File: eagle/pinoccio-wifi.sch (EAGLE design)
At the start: 23 parts, among them J1 AVR_SPI_PRG_6, J2 AVR_SPI_PRG_6, U1 GS1011MIPS, U2 M25PX16, U3 M25PX16, U4 TPS73533, U5 ATTINY13A

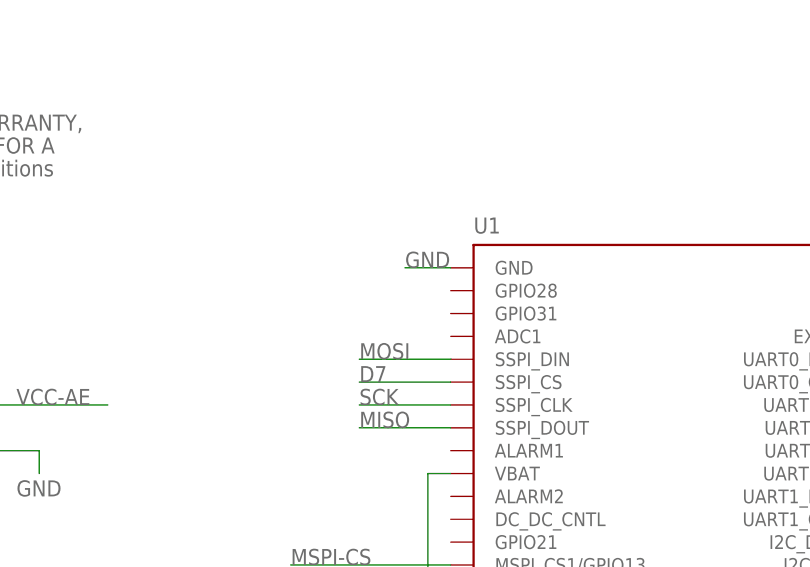
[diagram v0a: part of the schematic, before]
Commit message: Add data-ready trace to D5
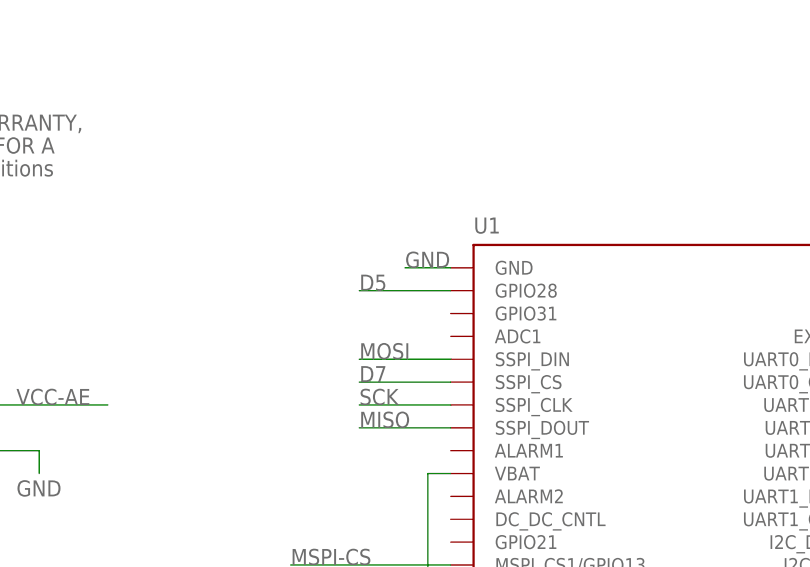
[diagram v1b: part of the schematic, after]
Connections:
- net D5: now also U1.GPIO28
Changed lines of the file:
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@@
 <label x="218.44" y="147.32" size="1.778" layer="95"/>
+</segment>
+<segment>
+<pinref part="U1" gate="GS1011MIPS" pin="GPIO28"/>
+<wire x1="134.62" y1="154.94" x2="124.46" y2="154.94" width="0.1524" layer="91"/>
+<label x="124.46" y="154.94" size="1.778" layer="95"/>
 </segment>
 </net>

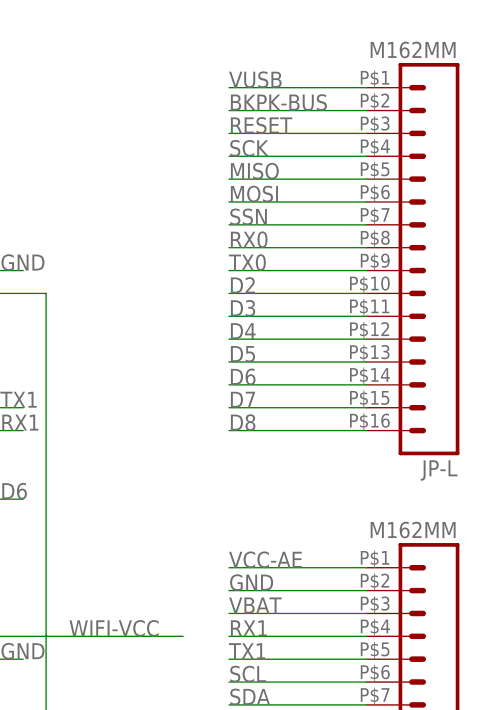
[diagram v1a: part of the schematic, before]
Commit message: Show component names and values on the PCB
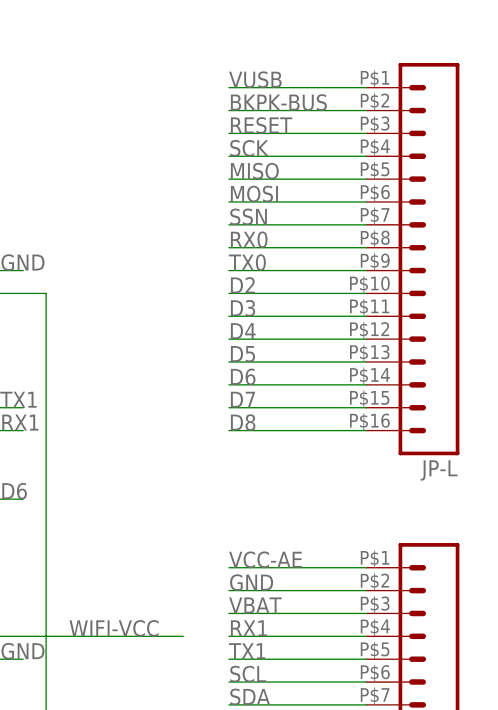
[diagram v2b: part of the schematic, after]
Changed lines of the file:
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@@
 <parts>
 <part name="FRAME1" library="Pinoccio" deviceset="FRAME-LETTER" device=""/>
-<part name="JP-R" library="Pinoccio" deviceset="M16" device="2MM"/>
-<part name="JP-L" library="Pinoccio" deviceset="M16" device="2MM"/>
+<part name="JP-R" library="Pinoccio" deviceset="M16" device="2MM" value=""/>
+<part name="JP-L" library="Pinoccio" deviceset="M16" device="2MM" value=""/>
 <part name="U1" library="Pinoccio" deviceset="GS1011MIPS" device=""/>
 <part name="U$1" library="Pinoccio" deviceset="MICROSD" device=""/>
